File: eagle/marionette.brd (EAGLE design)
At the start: 139.7 x 76.2 mm, 230 parts, among them J17 MA02-1, J18 MA02-1, J19 MA02-1, J2 SWD, J20 MA02-1, J22 ZX62D-B-5P8, J6 MA03-2W, J7 MA02-1, J8 MA04-2W, Q1 BSS84, U1 STM32F407, U10 LVM344, U12 AT24C04D, U13 CON_HIROSE_DM3D(MICROSD), U14 USB3320, U2 TC1262, U3 LM3671, U4 LK112, U5 MAX3051ESA, U6 DAC124S085CIMM, U7 LVM344, U8 LVM344, U9 LVM344, X1 ABSO7, X2 NX3225SA

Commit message: Added RC values for Anti-aliasing filters
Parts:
- C49, C50, C51, C52, C53, C54, C57, C58, C59, C60, C61, C62, C63, C64, C65, C66, C67, C68, C69, C70, C71, C72, C73, C74, C75, C76, C77, C78, C79, C80: value (none) -> 1nF
- R31, R32, R33, R34, R35, R36, R39, R40, R41, R42, R43, R44, R45, R46, R47, R48, R49, R50, R51, R52, R53, R54, R55, R56, R57, R58, R59, R60, R61, R62: value (none) -> 7.5k

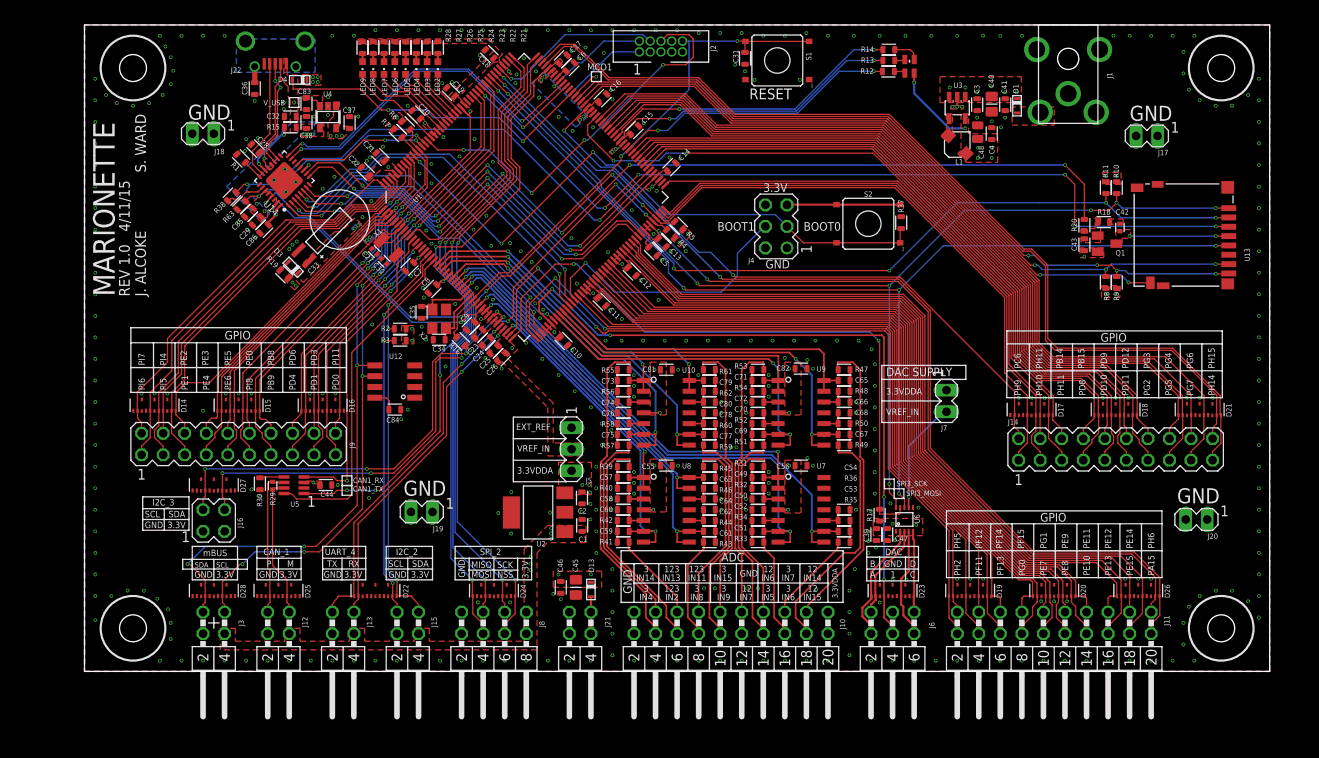
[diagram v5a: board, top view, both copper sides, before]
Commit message: Uh... some changes. Sorry Jeff. I realized I hadn't passed the layout by our 'customers', specifically Chris and a few other mfg engineers, and they wanted the spare headers wrapped around the edge of the board, not in the middle of the board. So I did that. Also added ground and power to the GPIO connectors, which is critical to usability. Also I fixed:
- Moved BOOT0 and BOOT0 jumper to near board edge (for mezannine stacking). Also cleaned up Jumper (only need to pull high).
- Removed BOOT1 jumper - we don't need it. We'll never (HA!) boot out of SRAM.
- Moved LED towards edge of board (for mezannine stacking)
- Replaced all 0402 packages with 0603s.
- Added un-invoked spare op-amp as a follower from the STM DAC1 !!11!!
- Removed an unused pin on VREFIN.
- Changed U2 3.3VDDA LDO input from 3.3VDD to VCC (5.0V).
- Need 5V out on the ECOD.
- Need power and ground on GPIO connectors.
- Zero ohm resistor on DAC ref

Still more to do (DRC checking, expanding out from design rules, ground stitching).
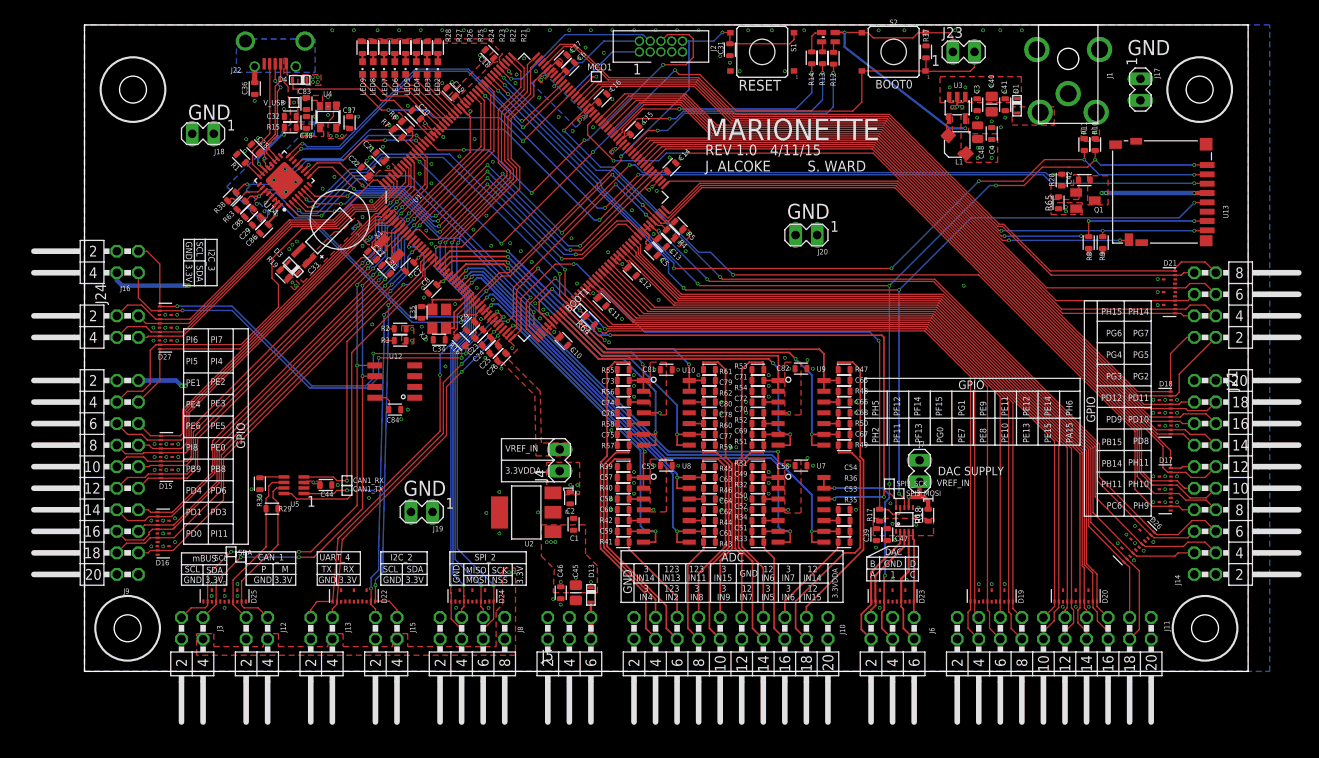
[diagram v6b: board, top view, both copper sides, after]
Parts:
- removed C43: 0.1uF, rcl_custom:.0603-C
- removed D14, D28: ESD8008, ESD8008MUT:UFDFN-14
- added BOOT1: TEST-POINT10MIL-TEST-POINT, Tova:10MIL-TEST-POINT
- added J23: MA02-1, MA_HEADER:MA02-1
- added J24: (no value), MA_HEADER:MA02-2W
- added R64: 10k, rcl_custom:.0603-C
- added R65: 100k, rcl_custom:.0603-C
- C27, C30, R29: device rcl_custom:.0402-C -> rcl_custom:.0603-C
- C34, C35: value 4.4nF -> 4.4p
- C42: value 10pF -> 100p; device rcl_custom:.0402-C -> rcl_custom:.0603-C
- J14, J9: device MA_HEADER:MA10-2 -> MA_HEADER:MA10-2W
- J16: device MA_HEADER:MA02-2 -> MA_HEADER:MA02-2W
- J21: value (none) -> MA04-2W; device MA_HEADER:MA02-2W -> MA_HEADER:MA04-2W
- J4: value (none) -> MA02-1; device MA_HEADER:MA03-2 -> MA_HEADER:MA02-1
- J5: value (none) -> MA03-2W; device MA_HEADER:MA03-1 -> MA_HEADER:MA03-2W
- R18: value 100 -> 0
- R20: value 60k -> 10k
- moved J21 82.6 mm to (132.1, 43.2), turned to 90 degrees
- moved J20 56.9 mm to (85.1, 51.4)
- moved R18 40.3 mm to (99.4, 18.4), turned to 90 degrees
- moved J4 37.6 mm to (56.0, 24.9)
- moved J16 32.1 mm to (5.08, 48.3), turned to 270 degrees
- moved D16 24.1 mm to (9.27, 16.3), turned to 270 degrees
- moved J5 21.1 mm to (57.1, 5.08), turned to 0 degrees
- moved S2 20.5 mm to (95.4, 73.0)
- moved R37 20.3 mm to (99.2, 73.0)
- moved D27 19.4 mm to (9.53, 40.5), turned to 270 degrees
- moved D17 18.3 mm to (127.4, 21.5), turned to 90 degrees
- moved D21 14.3 mm to (127.9, 44.7), turned to 90 degrees
- moved J9 13.7 mm to (5.08, 22.9), turned to 270 degrees
- moved J14 11.0 mm to (132.1, 22.9), turned to 90 degrees
- moved D15 10.5 mm to (9.65, 25.3), turned to 270 degrees
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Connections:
- net N$7 renamed SDIO-PWR-SWITCHED
- net N$8 renamed VBATT
- net PC15 renamed SDIO-PWR
- removed net N$24: C42.2, R18.2
- new net DAC1_FILT: D23.P3, J6.3, U7.13, U7.14
- net +3.3VDDA: now also J10.1, J10.2, J4.1, R18.1; no longer J10.19, J10.20, J5.3, J7.1
- net 3.3VDD: now also J11.1, J11.2, J23.1, J9.1, J9.2, R65.1; no longer C1.1, C43.1, J4.5, J4.6, U2.1
- net BOOT0: now also J23.2; no longer J4.3
- net BOOT1: now also BOOT1.P$1, R64.2; no longer J4.4
- net CAN1_M: now also D25.P7; no longer D25.P6
- net CAN1_P: now also D25.P6; no longer D25.P3
- net DAC1: now also U7.12; no longer D23.P3, J6.3
- net GND: now also J10.19, J10.20, J11.19, J11.20, J5.3, J5.4, J7.2, J9.19, J9.20, R64.1; no longer D14.GND@1, D14.GND@2, D14.GND@3, D14.GND@4, D14.GND@5, D14.GND@6, D28.GND@1, D28.GND@2, D28.GND@3, D28.GND@4, D28.GND@5, D28.GND@6, J10.1, J10.2, J21.1, J21.2, J4.1, J4.2
- net I2C1_SCL: now also D25.P3; no longer D28.P6
- net I2C1_SDA: now also D25.P2; no longer D28.P3
- net I2C3_SCL: now also D27.P1; no longer D27.P3
- net I2C3_SDA: now also D27.P2; no longer D27.P6
- net N$15: now also J7.1, R18.2; no longer J7.2
- net N$22: now also C42.2, R65.2; no longer C43.2, R18.1
- net N$6: now also J5.5, J5.6; no longer J21.3, J21.4
- net PA15: now also J14.5; no longer J11.19
- net PB15: now also J14.14; no longer J14.8
- net PB8: now also J9.12; no longer J9.14
- net PB9: now also J9.11; no longer J9.13
- net PC6: now also J14.8; no longer J14.2
- net PD0: now also J9.17; no longer J9.19
- net PD1: now also J9.15; no longer J9.17
- net PD10: now also J14.15; no longer J14.9
- net PD11: now also J14.17; no longer J14.11
- net PD12: now also J14.18; no longer J14.12
- net PD3: now also J9.16; no longer J9.18
- net PD4: now also J9.13; no longer J9.15
- net PD6: now also J9.14; no longer J9.16
- net PD8: now also J14.13; no longer J14.7
- net PD9: now also J14.16; no longer J14.10
- net PE0: now also J9.10; no longer J9.12
- net PE1: now also D27.P7, J9.3; no longer D14.P7, J9.5
- net PE10: now also J11.15; no longer J11.13
- net PE11: now also J11.16; no longer J11.14
- net PE12: now also J11.18; no longer J11.16
- net PE13: now also J11.17; no longer J11.15
- net PE14: now also J14.4; no longer J11.18
- net PE15: now also J14.3; no longer J11.17
- net PE2: now also D27.P8, J9.4; no longer D14.P8, J9.6
- net PE3: now also J9.6; no longer J9.8
- net PE4: now also J9.5; no longer J9.7
- net PE5: now also J9.8; no longer J9.10
- net PE6: now also J9.7; no longer J9.9
- net PE7: now also J11.11; no longer J11.9
- net PE8: now also J11.13; no longer J11.11
- net PE9: now also J11.14; no longer J11.12
- net PF11: now also J11.5; no longer J11.3
- net PF12: now also J11.6; no longer J11.4
- net PF13: now also J11.7; no longer J11.5
- net PF14: now also J11.8; no longer J11.6
- net PF15: now also J11.10; no longer J11.8
- net PG0: now also J11.9; no longer J11.7
- net PG1: now also J11.12; no longer J11.10
- net PG2: now also J21.1; no longer J14.13
- net PG3: now also J21.2; no longer J14.14
- net PG4: now also J21.4; no longer J14.16
- net PG5: now also J21.3; no longer J14.15
- net PG6: now also J21.6; no longer J14.18
- net PG7: now also J21.5; no longer J14.17
- net PG8: now also J14.12; no longer J14.6
- net PH10: now also J14.9; no longer J14.3
- net PH11: now also J14.10; no longer J14.4
- net PH12: now also J14.11; no longer J14.5
- net PH14: now also J21.8; no longer J14.20
- net PH15: now also J21.7; no longer J14.19
- net PH2: now also J11.3; no longer J11.1
- net PH5: now also J11.4; no longer J11.2
- net PH6: now also J14.6; no longer J11.20
- net PH9: now also J14.7; no longer J14.1
- net PI11: now also J9.18; no longer J9.20
- net PI4: now also D27.P6, J24.4; no longer D14.P6, J9.4
- net PI5: now also D27.P5, J24.3; no longer D14.P5, J9.3
- net PI6: now also D27.P4, J24.2; no longer D14.P4, J9.1
- net PI7: now also D27.P3, J24.1; no longer D14.P2, J9.2
- net PI8: now also J9.9; no longer J9.11
- net VCC: now also C1.1, J5.1, J5.2, U2.1
- net VREF+: now also J4.2; no longer J5.2
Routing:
- net 3.3VDD: track 42.8 -> 75.5 mm, vias 52 -> 54
- net BOOT1: track 32.6 -> 2.53 mm, vias 1 -> 0
- net DAC1_FILT: track 0.00 -> 27.2 mm, vias 0 -> 2
- net PI11: track 26.3 -> 52.2 mm
- net PC6: track 75.5 -> 100.7 mm
- net PD0: track 52.8 -> 77.1 mm
- net PD1: track 52.8 -> 75.8 mm
- net PD3: track 48.8 -> 71.0 mm
- net PD4: track 51.9 -> 72.3 mm
- net PD6: track 47.5 -> 66.9 mm
- net PH14: track 107.5 -> 88.7 mm
- net PH15: track 111.0 -> 92.5 mm
- net PH9: track 68.7 -> 86.5 mm
- net PH10: track 69.3 -> 85.8 mm
- net BOOT0: track 72.4 -> 88.6 mm, vias 3 -> 4
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- removed copper zone on layer 1, net N$24
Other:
- board size 139.7 x 76.2 mm -> 137.2 x 76.2 mm
- board text removed: "BOOT1"
- board text removed: "EXT_REF"

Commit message: Did more on the board:
- ZERO OHM RESISTOR ON JUMPERS
- Fixed power and bypass cap to on-board EEPROM
- Added 10 uF cap to uSD card.
- Added more bypass to power supplies (0805 10u and 0603 100n to various supplies)
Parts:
- added A1, A2: TEST-POINT10MIL-TEST-POINT, Tova:10MIL-TEST-POINT
- added C43: 10u, rcl_custom:.0805-C-NOSILK
- added C87, C89, C90: 100n, rcl_custom:.0603-C
- added C88: 4.7u, rcl_custom:.0805-C-NOSILK
- added R66, R67: 10k, rcl_custom:.0603-C
- C1: value 1uF -> 4.7u; device rcl_custom:.0603-C -> rcl_custom:.0805-C-NOSILK
- C10, C12, C13, C14, C15, C16, C17, C18, C19, C20, C21, C24, C26, C31, C7, C8, C9: value .1uF -> 100n
- C11: value .1uf -> 100n
- C2, C25, C41, C46: value 1uF -> 100n
- C22, C3: value 4.7uF -> 4.7u; device rcl_custom:.0603-C -> rcl_custom:.0805-C-NOSILK
- C23, C37, C55, C56, C81, C82: value 1uF -> 1u
- C28: value 2.2uF, 10V -> 2.2u
- C29, C85, C86: value 100nF, 10V -> 100n
- C32: value 1uF, 10V -> 1u
- C33: value 220mF -> 220m
- C36: value 0.1uF, 10V -> 100n 50V
- C38, C5, C6: value 2.2uF -> 2.2u
- C39: value 10uF -> 10u; device rcl_custom:.0603-C -> rcl_custom:.0805-C-NOSILK
- C4: value 1uf -> 100n
- C40, C45: value 10uF -> 10u; device rcl_custom:.0805-B -> rcl_custom:.0805-C-NOSILK
- C44, C47, C83: value 0.1uF -> 100n
- C48: value 10uf -> 10u
- C49, C50, C51, C52, C53, C54, C57, C58, C59, C60, C61, C62, C63, C64, C65, C66, C67, C68, C69, C70, C71, C72, C73, C74, C75, C76, C77, C78, C79, C80: value 1nF -> 1n
- C84: value NP -> 100n
- R17: value 4.7k -> 10k
- moved C39 5.99 mm to (99.3, 15.6)
- moved D13 5.64 mm to (57.5, 14.2)
- moved C41 5.26 mm to (112.0, 62.9)
- moved C1 5.03 mm to (53.6, 14.4), turned to 180 degrees
- moved C40 4.91 mm to (110.1, 63.1)
- moved C47 4.89 mm to (98.9, 18.4), turned to 90 degrees
- moved C4 2.64 mm to (105.4, 65.6)
- moved J4 2.62 mm to (57.3, 27.2), turned to 0 degrees
- moved C46 2.52 mm to (58.0, 10.9), turned to 180 degrees
- moved C3 2.10 mm to (107.3, 66.9)
- moved C48 2.05 mm to (107.3, 63.3)
- moved J7 1.48 mm to (99.7, 24.4), turned to 0 degrees
- moved R18 0.76 mm to (100.2, 18.4)
- moved C2 0.48 mm to (57.5, 20.1)
- moved C45 0.28 mm to (58.0, 9.02), turned to 180 degrees
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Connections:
- removed net N$45: C84.1, U12.8
- removed net N$6: D13.P$1, J5.5, J5.6
- new net VEXT-COAX: C40.1, C41.1, D1.P$1, J1.1
- new net VEXT-ECOD: C45.1, C46.1, D13.P$1, J5.5, J5.6
- net +3.3VDDA: now also C88.1, R66.2; no longer J4.1
- net 3.3VDD: now also C84.1, J14.1, J14.2, U12.8
- net GND: now also A1.P$1, A2.P$1, C43.2, C87.2, C88.2, C89.2, C90.2, D17.P1, D17.P3, D19.P3, D19.P5, D21.P4, D21.P6, D26.P4, D26.P6, J14.19, J14.20, J4.2; no longer J1.3
- net N$1: now also R67.2, U3.3; no longer D1.P$1, J1.1
- net N$15: now also C90.1
- net SDIO-PWR-SWITCHED: now also C43.1
- net VCC: now also C87.1, C89.1, R67.1; no longer C40.1, C41.1, C45.1, C46.1, U3.3
- net VREF+: now also J4.1, R66.1; no longer J4.2
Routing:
- net N$6: track 4.48 -> 0.00 mm
- net N$15: track 6.55 -> 10.6 mm, vias 1 -> 0
- net N$45: track 2.92 -> 0.00 mm
- net N$1: track 0.00 -> 1.28 mm
- net GND: track 5.84 -> 6.86 mm, vias 258 -> 280
- net VCC: track 0.00 -> 0.70 mm, vias 16 -> 24
- net 3.3VDD: track 75.5 -> 75.6 mm, vias 54 -> 63
- net +3.3VDDA: vias 15 -> 14
- added copper zone on layer 1, net VEXT-COAX
- added copper zone on layer 1, net VEXT-ECOD
- added copper zone on layer 16, net VEXT-ECOD
- removed copper zone on layer 1, net N$1

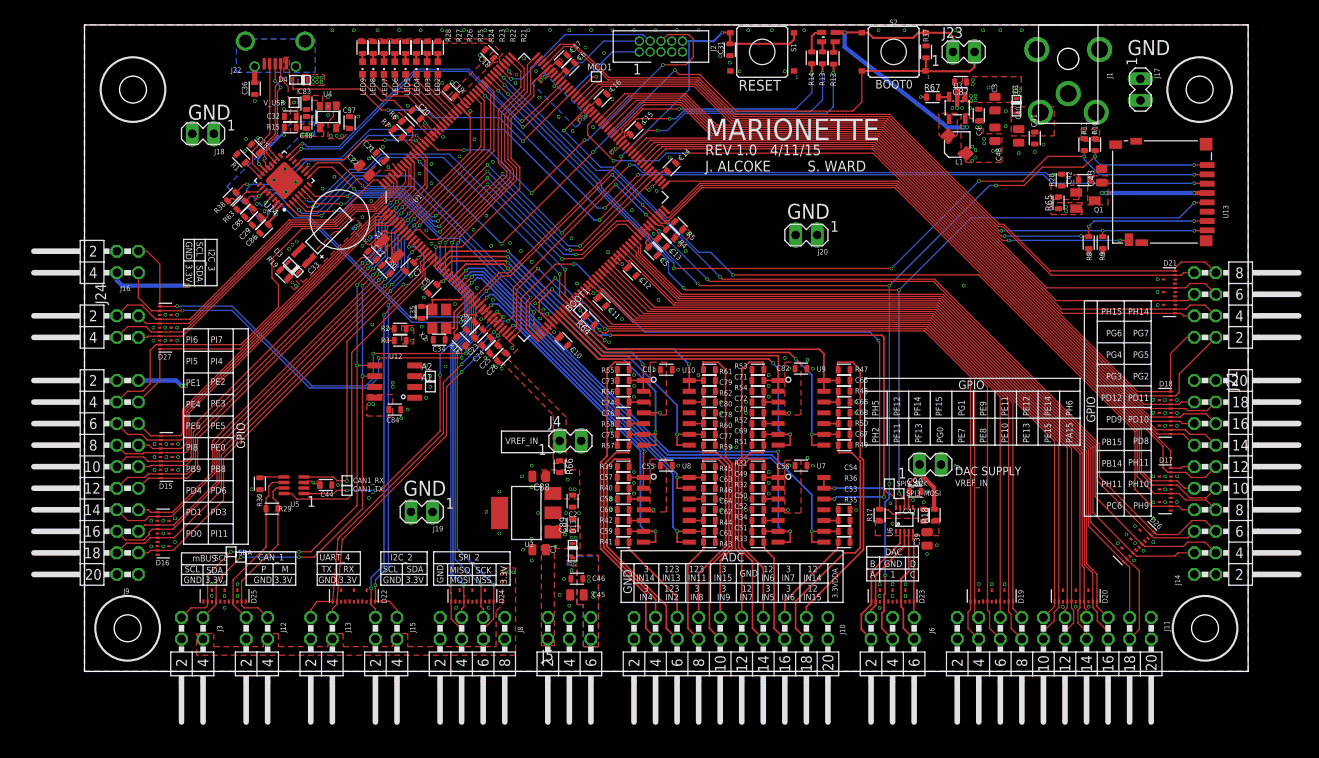
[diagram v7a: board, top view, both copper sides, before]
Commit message: Ground stitching, final checks. Back to Jeff for tsilk cleanup.
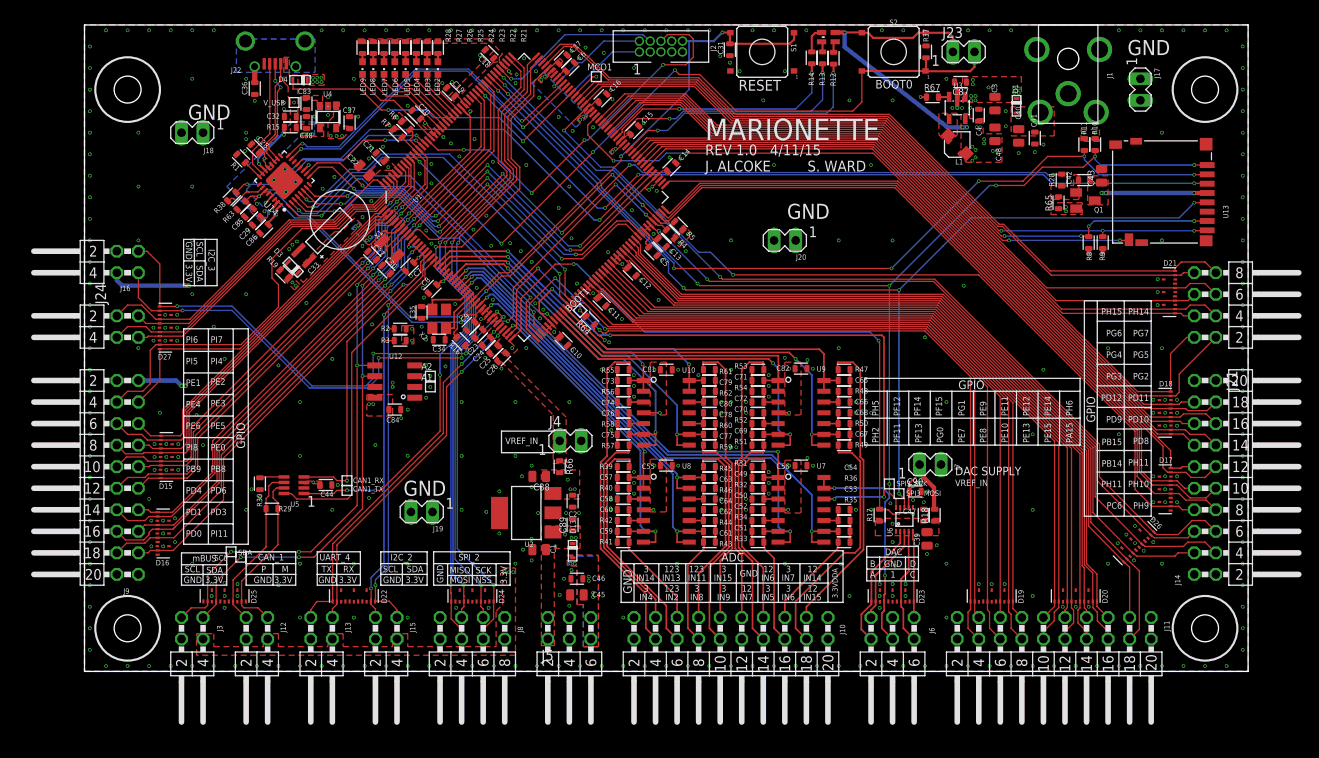
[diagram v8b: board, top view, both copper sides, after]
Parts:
- moved J20 2.62 mm to (82.5, 50.8)
- moved J18 1.28 mm to (12.7, 63.5)
- moved U$34 0.64 mm to (132.1, 68.6)
- moved U$36 0.63 mm to (5.08, 68.6)
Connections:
- net N$36 renamed SHLD
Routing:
- net GND: vias 280 -> 490
